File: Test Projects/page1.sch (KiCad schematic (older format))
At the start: 21 parts, among them P1 CONN_01X02, U1 LDO-adj-4term, U2 Teensy_3.2, U3 LDO-adj-4term, U6 LDO-adj-4term

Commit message: Tested a few layout sections
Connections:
- net Bulk_IN: now reaches C1.1, C12.1, C4.1, P1.1 (P1), U1.3 (IN), U3.3 (IN), U6.3 (IN)
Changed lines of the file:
@@
 Connection ~ 4850 4450
 Connection ~ 4850 4550
+Text Label 1950 2800 1    50   ~ 0
+Bulk_IN
 $EndSCHEMATC

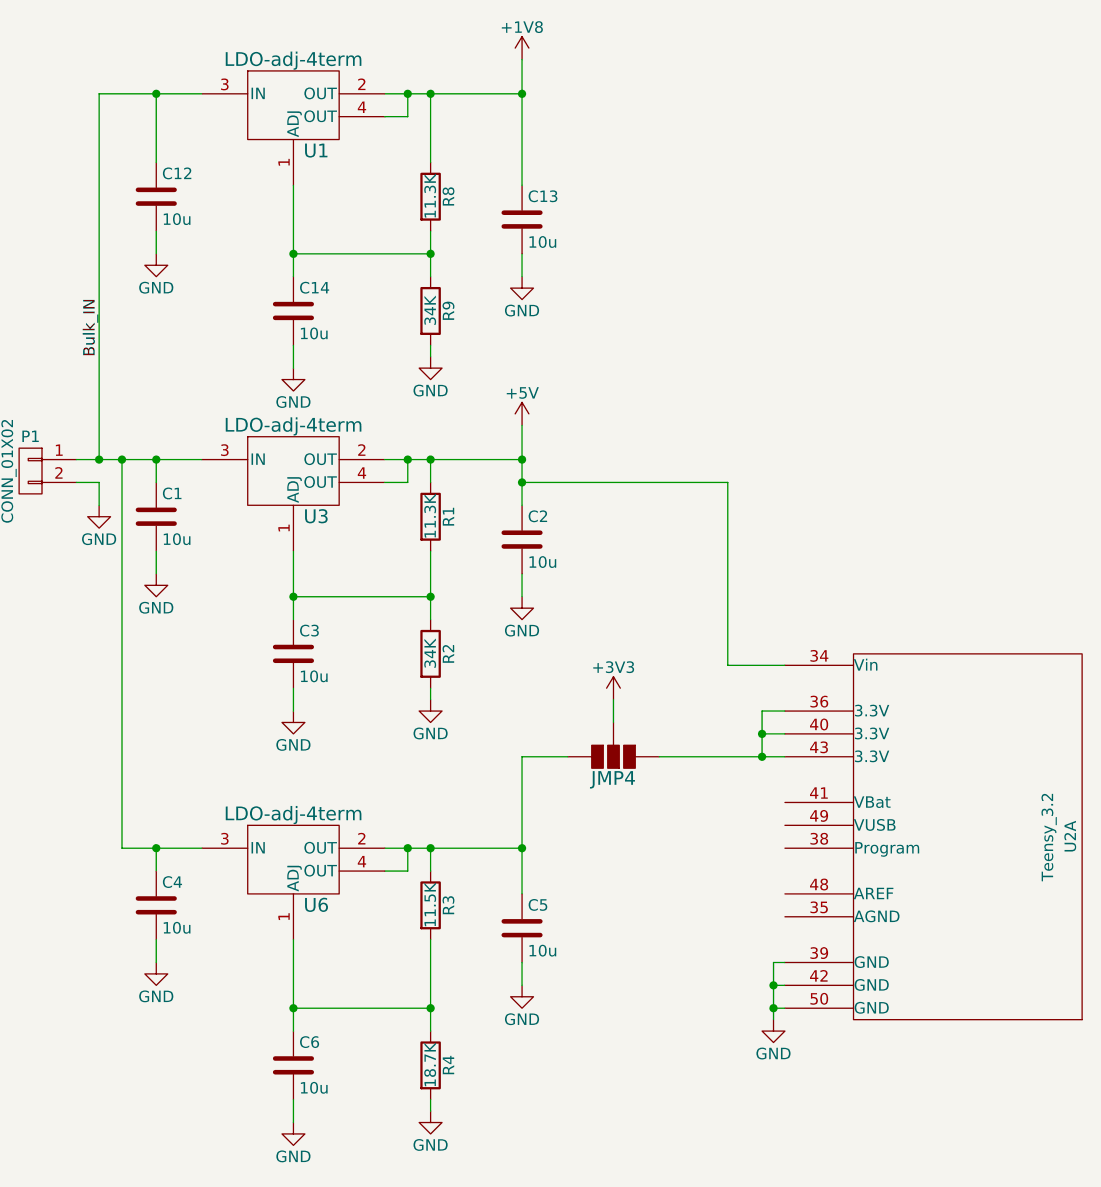
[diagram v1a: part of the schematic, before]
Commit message: Moved to 10x5 size
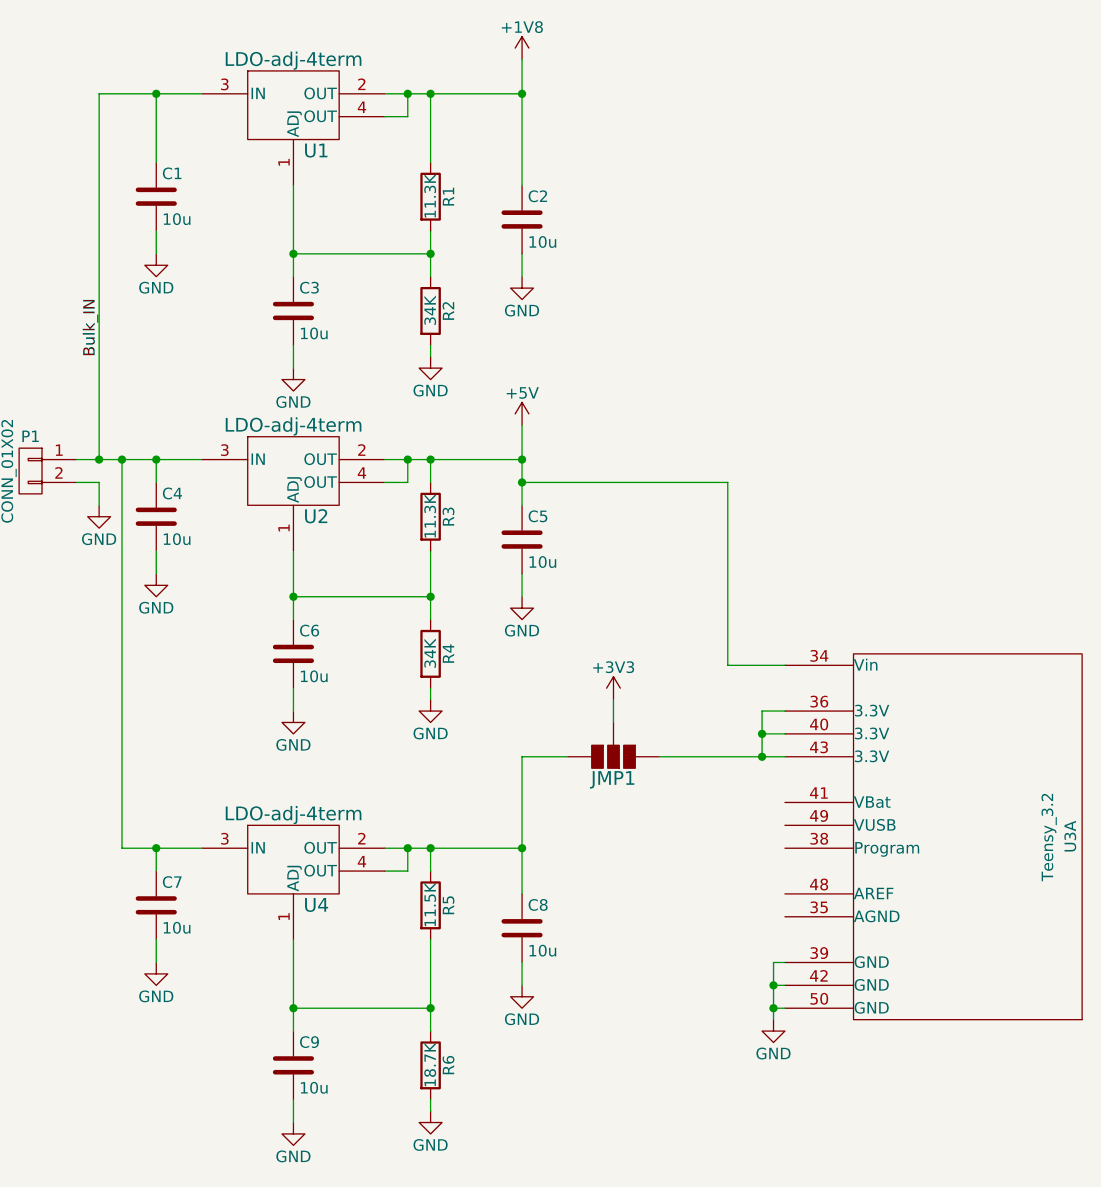
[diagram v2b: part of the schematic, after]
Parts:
- renumbered C12 to C1, C13 to C2, C14 to C3, C1 to C4, C2 to C5, C3 to C6, C4 to C7, C5 to C8, C6 to C9, JMP4 to JMP1, R8 to R1, R9 to R2, R1 to R3, R2 to R4, R3 to R5, R4 to R6, U3 to U2, U2 to U3, U6 to U4
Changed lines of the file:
@@
 $EndDescr
 $Comp
-L Teensy_3.2 U2
+L Teensy_3.2 U3
 U 1 1 56886AFB
 P 5750 4900
-F 0 "U2" V 6200 4900 50  0000 C CNN
+F 0 "U3" V 6200 4900 50  0000 C CNN
 F 1 "Teensy_3.2" V 6100 4900 50  0000 C CNN
 F 2 "teensy footprints:Teensy_3.2_Route" H 5450 5200 50  0001 C CNN
@@
 $EndComp
 $Comp
-L R R2
+L R R4
 U 1 1 568870D8
 P 3400 4100
-F 0 "R2" V 3480 4100 50  0000 C CNN
+F 0 "R4" V 3480 4100 50  0000 C CNN
 F 1 "34K" V 3400 4100 50  0000 C CNN
 F 2 "Resistors_SMD:R_0603" V 3330 4100 50  0001 C CNN
@@
 $EndComp
 $Comp
-L R R1
+L R R3
 U 1 1 568871A2
 P 3400 3500
-F 0 "R1" V 3480 3500 50  0000 C CNN
+F 0 "R3" V 3480 3500 50  0000 C CNN
 F 1 "11.3K" V 3400 3500 50  0000 C CNN
 F 2 "Resistors_SMD:R_0603" V 3330 3500 50  0001 C CNN
@@
 $EndComp
 $Comp
-L R R3
+L R R5
 U 1 1 568871E0
 P 3400 5200
-F 0 "R3" V 3480 5200 50  0000 C CNN
+F 0 "R5" V 3480 5200 50  0000 C CNN
 F 1 "11.5K" V 3400 5200 50  0000 C CNN
 F 2 "Resistors_SMD:R_0603" V 3330 5200 50  0001 C CNN
@@
 $EndComp
 $Comp
-L R R4
+L R R6
 U 1 1 56887253
 P 3400 5900
-F 0 "R4" V 3480 5900 50  0000 C CNN
+F 0 "R6" V 3480 5900 50  0000 C CNN
 F 1 "18.7K" V 3400 5900 50  0000 C CNN
 F 2 "Resistors_SMD:R_0603" V 3330 5900 50  0001 C CNN
@@
 	1950 3350 1950 3450
 $Comp
-L C C2
+L C C5
 U 1 1 56887A60
 P 3800 3600
-F 0 "C2" H 3825 3700 50  0000 L CNN
+F 0 "C5" H 3825 3700 50  0000 L CNN
 F 1 "10u" H 3825 3500 50  0000 L CNN
 F 2 "Capacitors_Tantalum_SMD:TantalC_SizeB_EIA-3528_Reflow" H 3838 3450 50  0001 C CNN
@@
 $EndComp
 $Comp
-L C C5
+L C C8
 U 1 1 56887ACC
 P 3800 5300
-F 0 "C5" H 3825 5400 50  0000 L CNN
+F 0 "C8" H 3825 5400 50  0000 L CNN
 F 1 "10u" H 3825 5200 50  0000 L CNN
 F 2 "Capacitors_Tantalum_SMD:TantalC_SizeB_EIA-3528_Reflow" H 3838 5150 50  0001 C CNN
@@
 $EndComp
 $Comp
-L C C1
+L C C4
 U 1 1 56887B40
 P 2200 3500
-F 0 "C1" H 2225 3600 50  0000 L CNN
+F 0 "C4" H 2225 3600 50  0000 L CNN
 F 1 "10u" H 2225 3400 50  0000 L CNN
 F 2 "Capacitors_Tantalum_SMD:TantalC_SizeB_EIA-3528_Reflow" H 2238 3350 50  0001 C CNN
@@
 $EndComp
 $Comp
-L C C4
+L C C7
 U 1 1 56887BDF
 P 2200 5200
-F 0 "C4" H 2225 5300 50  0000 L CNN
+F 0 "C7" H 2225 5300 50  0000 L CNN
 F 1 "10u" H 2225 5100 50  0000 L CNN
 F 2 "Capacitors_Tantalum_SMD:TantalC_SizeB_EIA-3528_Reflow" H 2238 5050 50  0001 C CNN
@@
 $EndComp
 $Comp
-L C C6
+L C C9
 U 1 1 56887C61
 P 2800 5900
-F 0 "C6" H 2825 6000 50  0000 L CNN
+F 0 "C9" H 2825 6000 50  0000 L CNN
 F 1 "10u" H 2825 5800 50  0000 L CNN
 F 2 "Capacitors_Tantalum_SMD:TantalC_SizeB_EIA-3528_Reflow" H 2838 5750 50  0001 C CNN
@@
 $EndComp
 $Comp
-L C C3
+L C C6
 U 1 1 56887CBC
 P 2800 4100
-F 0 "C3" H 2825 4200 50  0000 L CNN
+F 0 "C6" H 2825 4200 50  0000 L CNN
 F 1 "10u" H 2825 4000 50  0000 L CNN
 F 2 "Capacitors_Tantalum_SMD:TantalC_SizeB_EIA-3528_Reflow" H 2838 3950 50  0001 C CNN
@@
 	2800 4350 2800 4250
 $Comp
-L R R9
+L R R2
 U 1 1 5687E4C2
 P 3400 2600
-F 0 "R9" V 3480 2600 50  0000 C CNN
+F 0 "R2" V 3480 2600 50  0000 C CNN
 F 1 "34K" V 3400 2600 50  0000 C CNN
 F 2 "Resistors_SMD:R_0603" V 3330 2600 50  0001 C CNN
@@
 $EndComp
 $Comp
-L R R8
+L R R1
 U 1 1 5687E4C8
 P 3400 2100
-F 0 "R8" V 3480 2100 50  0000 C CNN
+F 0 "R1" V 3480 2100 50  0000 C CNN
 F 1 "11.3K" V 3400 2100 50  0000 C CNN
 F 2 "Resistors_SMD:R_0603" V 3330 2100 50  0001 C CNN
@@
 	3400 2750 3400 2800
 $Comp
-L C C13
+L C C2
 U 1 1 5687E4DC
 P 3800 2200
-F 0 "C13" H 3825 2300 50  0000 L CNN
+F 0 "C2" H 3825 2300 50  0000 L CNN
 F 1 "10u" H 3825 2100 50  0000 L CNN
 F 2 "Capacitors_Tantalum_SMD:TantalC_SizeB_EIA-3528_Reflow" H 3838 2050 50  0001 C CNN
@@
 $EndComp
 $Comp
-L C C14
+L C C3
 U 1 1 5687E4E2
 P 2800 2600
-F 0 "C14" H 2825 2700 50  0000 L CNN
+F 0 "C3" H 2825 2700 50  0000 L CNN
 F 1 "10u" H 2825 2500 50  0000 L CNN
 F 2 "Capacitors_Tantalum_SMD:TantalC_SizeB_EIA-3528_Reflow" H 2838 2450 50  0001 C CNN
@@
 	1950 1650 2400 1650
 $Comp
-L C C12
+L C C1
 U 1 1 5687E55B
 P 2200 2100
-F 0 "C12" H 2225 2200 50  0000 L CNN
+F 0 "C1" H 2225 2200 50  0000 L CNN
 F 1 "10u" H 2225 2000 50  0000 L CNN
 F 2 "Capacitors_Tantalum_SMD:TantalC_SizeB_EIA-3528_Reflow" H 2238 1950 50  0001 C CNN
@@
 Connection ~ 3300 1650
 $Comp
-L LDO-adj-4term U3
+L LDO-adj-4term U2
 U 1 1 5687EBBA
 P 2800 3250
-F 0 "U3" H 2900 3000 60  0000 C CNN
+F 0 "U2" H 2900 3000 60  0000 C CNN
 F 1 "LDO-adj-4term" H 2800 3400 60  0000 C CNN
 F 2 "SparkFun-Footprints:SF-SOT-223" H 2800 3250 60  0001 C CNN
@@
 $EndComp
 $Comp
-L LDO-adj-4term U6
+L LDO-adj-4term U4
 U 1 1 5687EC39
 P 2800 4950
-F 0 "U6" H 2900 4700 60  0000 C CNN
+F 0 "U4" H 2900 4700 60  0000 C CNN
 F 1 "LDO-adj-4term" H 2800 5100 60  0000 C CNN
 F 2 "SparkFun-Footprints:SF-SOT-223" H 2800 4950 60  0001 C CNN
@@
 Connection ~ 3800 3250
 $Comp
-L 3Jumper JMP4
+L 3Jumper JMP1
 U 1 1 56882BB5
 P 4200 4550
-F 0 "JMP4" H 4200 4645 60  0000 C CNN
+F 0 "JMP1" H 4200 4645 60  0000 C CNN
 F 1 "3Jumper" H 4200 4735 60  0001 C CNN
 F 2 "SparkFun-Footprints:SF-3way-open" H 5355 4620 60  0001 C CNN

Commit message: First major routing pass
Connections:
- net +3V3_REG: now reaches C8.1, JMP1.3, R5.1, U4.2 (OUT), U4.4 (OUT)
- net +3V3_TOUT: now reaches JMP1.1, U3.36 (3.3V), U3.40 (3.3V), U3.43 (3.3V)
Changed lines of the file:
@@
 Connection ~ 2050 3250
 $Comp
-L GND #PWR1
+L GND #PWR01
 U 1 1 56887438
 P 1950 3450
-F 0 "#PWR1" H 1950 3200 50  0001 C CNN
+F 0 "#PWR01" H 1950 3200 50  0001 C CNN
 F 1 "GND" H 1950 3300 50  0000 C CNN
 F 2 "" H 1950 3450 50  0000 C CNN
@@
 $EndComp
 $Comp
-L GND #PWR9
+L GND #PWR02
 U 1 1 56887462
 P 3400 4300
-F 0 "#PWR9" H 3400 4050 50  0001 C CNN
+F 0 "#PWR02" H 3400 4050 50  0001 C CNN
 F 1 "GND" H 3400 4150 50  0000 C CNN
 F 2 "" H 3400 4300 50  0000 C CNN
@@
 $EndComp
 $Comp
-L GND #PWR10
+L GND #PWR03
 U 1 1 56887485
 P 3400 6100
-F 0 "#PWR10" H 3400 5850 50  0001 C CNN
+F 0 "#PWR03" H 3400 5850 50  0001 C CNN
 F 1 "GND" H 3400 5950 50  0000 C CNN
 F 2 "" H 3400 6100 50  0000 C CNN
@@
 $EndComp
 $Comp
-L GND #PWR17
+L GND #PWR04
 U 1 1 568874A8
 P 4900 5700
-F 0 "#PWR17" H 4900 5450 50  0001 C CNN
+F 0 "#PWR04" H 4900 5450 50  0001 C CNN
 F 1 "GND" H 4900 5550 50  0000 C CNN
 F 2 "" H 4900 5700 50  0000 C CNN
@@
 $EndComp
 $Comp
-L GND #PWR14
+L GND #PWR05
 U 1 1 56887D2E
 P 3800 3850
-F 0 "#PWR14" H 3800 3600 50  0001 C CNN
+F 0 "#PWR05" H 3800 3600 50  0001 C CNN
 F 1 "GND" H 3800 3700 50  0000 C CNN
 F 2 "" H 3800 3850 50  0000 C CNN
@@
 $EndComp
 $Comp
-L GND #PWR15
+L GND #PWR06
 U 1 1 56887D63
 P 3800 5550
-F 0 "#PWR15" H 3800 5300 50  0001 C CNN
+F 0 "#PWR06" H 3800 5300 50  0001 C CNN
 F 1 "GND" H 3800 5400 50  0000 C CNN
 F 2 "" H 3800 5550 50  0000 C CNN
@@
 $EndComp
 $Comp
-L GND #PWR7
+L GND #PWR07
 U 1 1 56887D98
 P 2800 6150
-F 0 "#PWR7" H 2800 5900 50  0001 C CNN
+F 0 "#PWR07" H 2800 5900 50  0001 C CNN
 F 1 "GND" H 2800 6000 50  0000 C CNN
 F 2 "" H 2800 6150 50  0000 C CNN
@@
 $EndComp
 $Comp
-L GND #PWR4
+L GND #PWR08
 U 1 1 56887DCD
 P 2200 5450
-F 0 "#PWR4" H 2200 5200 50  0001 C CNN
+F 0 "#PWR08" H 2200 5200 50  0001 C CNN
 F 1 "GND" H 2200 5300 50  0000 C CNN
 F 2 "" H 2200 5450 50  0000 C CNN
@@
 $EndComp
 $Comp
-L GND #PWR3
+L GND #PWR09
 U 1 1 56887E02
 P 2200 3750
-F 0 "#PWR3" H 2200 3500 50  0001 C CNN
+F 0 "#PWR09" H 2200 3500 50  0001 C CNN
 F 1 "GND" H 2200 3600 50  0000 C CNN
 F 2 "" H 2200 3750 50  0000 C CNN
@@
 Connection ~ 2800 3850
 $Comp
-L GND #PWR6
+L GND #PWR010
 U 1 1 56888143
 P 2800 4350
-F 0 "#PWR6" H 2800 4100 50  0001 C CNN
+F 0 "#PWR010" H 2800 4100 50  0001 C CNN
 F 1 "GND" H 2800 4200 50  0000 C CNN
 F 2 "" H 2800 4350 50  0000 C CNN
@@
 Connection ~ 3400 1650
 $Comp
-L GND #PWR8
+L GND #PWR011
 U 1 1 5687E4D5
 P 3400 2800
-F 0 "#PWR8" H 3400 2550 50  0001 C CNN
+F 0 "#PWR011" H 3400 2550 50  0001 C CNN
 F 1 "GND" H 3400 2650 50  0000 C CNN
 F 2 "" H 3400 2800 50  0000 C CNN
@@
 $EndComp
 $Comp
-L GND #PWR12
+L GND #PWR012
 U 1 1 5687E4E8
 P 3800 2450
-F 0 "#PWR12" H 3800 2200 50  0001 C CNN
+F 0 "#PWR012" H 3800 2200 50  0001 C CNN
 F 1 "GND" H 3800 2300 50  0000 C CNN
 F 2 "" H 3800 2450 50  0000 C CNN
@@
 Connection ~ 2800 2350
 $Comp
-L GND #PWR5
+L GND #PWR013
 U 1 1 5687E4F2
 P 2800 2850
-F 0 "#PWR5" H 2800 2600 50  0001 C CNN
+F 0 "#PWR013" H 2800 2600 50  0001 C CNN
 F 1 "GND" H 2800 2700 50  0000 C CNN
 F 2 "" H 2800 2850 50  0000 C CNN
@@
 $EndComp
 $Comp
-L GND #PWR2
+L GND #PWR014
 U 1 1 5687E561
 P 2200 2350
-F 0 "#PWR2" H 2200 2100 50  0001 C CNN
+F 0 "#PWR014" H 2200 2100 50  0001 C CNN
 F 1 "GND" H 2200 2200 50  0000 C CNN
 F 2 "" H 2200 2350 50  0000 C CNN
@@
 Connection ~ 1950 3250
 $Comp
-L +3V3 #PWR16
+L +3V3 #PWR015
 U 1 1 5687F792
 P 4200 4300
-F 0 "#PWR16" H 4200 4150 50  0001 C CNN
+F 0 "#PWR015" H 4200 4150 50  0001 C CNN
 F 1 "+3V3" H 4200 4440 50  0000 C CNN
 F 2 "" H 4200 4300 50  0000 C CNN
@@
 $EndComp
 $Comp
-L +1V8 #PWR11
+L +1V8 #PWR016
 U 1 1 5687F99A
 P 3800 1500
-F 0 "#PWR11" H 3800 1350 50  0001 C CNN
+F 0 "#PWR016" H 3800 1350 50  0001 C CNN
 F 1 "+1V8" H 3800 1640 50  0000 C CNN
 F 2 "" H 3800 1500 50  0000 C CNN
@@
 $EndComp
 $Comp
-L +5V #PWR13
+L +5V #PWR017
 U 1 1 56881FFF
 P 3800 3100
-F 0 "#PWR13" H 3800 2950 50  0001 C CNN
+F 0 "#PWR017" H 3800 2950 50  0001 C CNN
 F 1 "+5V" H 3800 3240 50  0000 C CNN
 F 2 "" H 3800 3100 50  0000 C CNN
@@
 Text Label 1950 2800 1    50   ~ 0
 Bulk_IN
+Text GLabel 3800 4700 0    50   UnSpc ~ 0
++3V3_REG
+Text GLabel 4850 4350 0    50   UnSpc ~ 0
++3V3_TOUT
 $EndSCHEMATC
